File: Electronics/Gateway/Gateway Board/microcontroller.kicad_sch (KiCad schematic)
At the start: 57 parts, among them IC301 STM32H723ZGT6, IC302 TJA1057GT/3, IC303 TJA1057GT/3, IC304 TJA1057GT/3, J301 TC2030, J302 MEM2075-00-140-01-A, J303 TYPE-C-31-M-12, J304 Screw_Terminal_01x02, J305 Screw_Terminal_01x02, J306 Screw_Terminal_01x02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

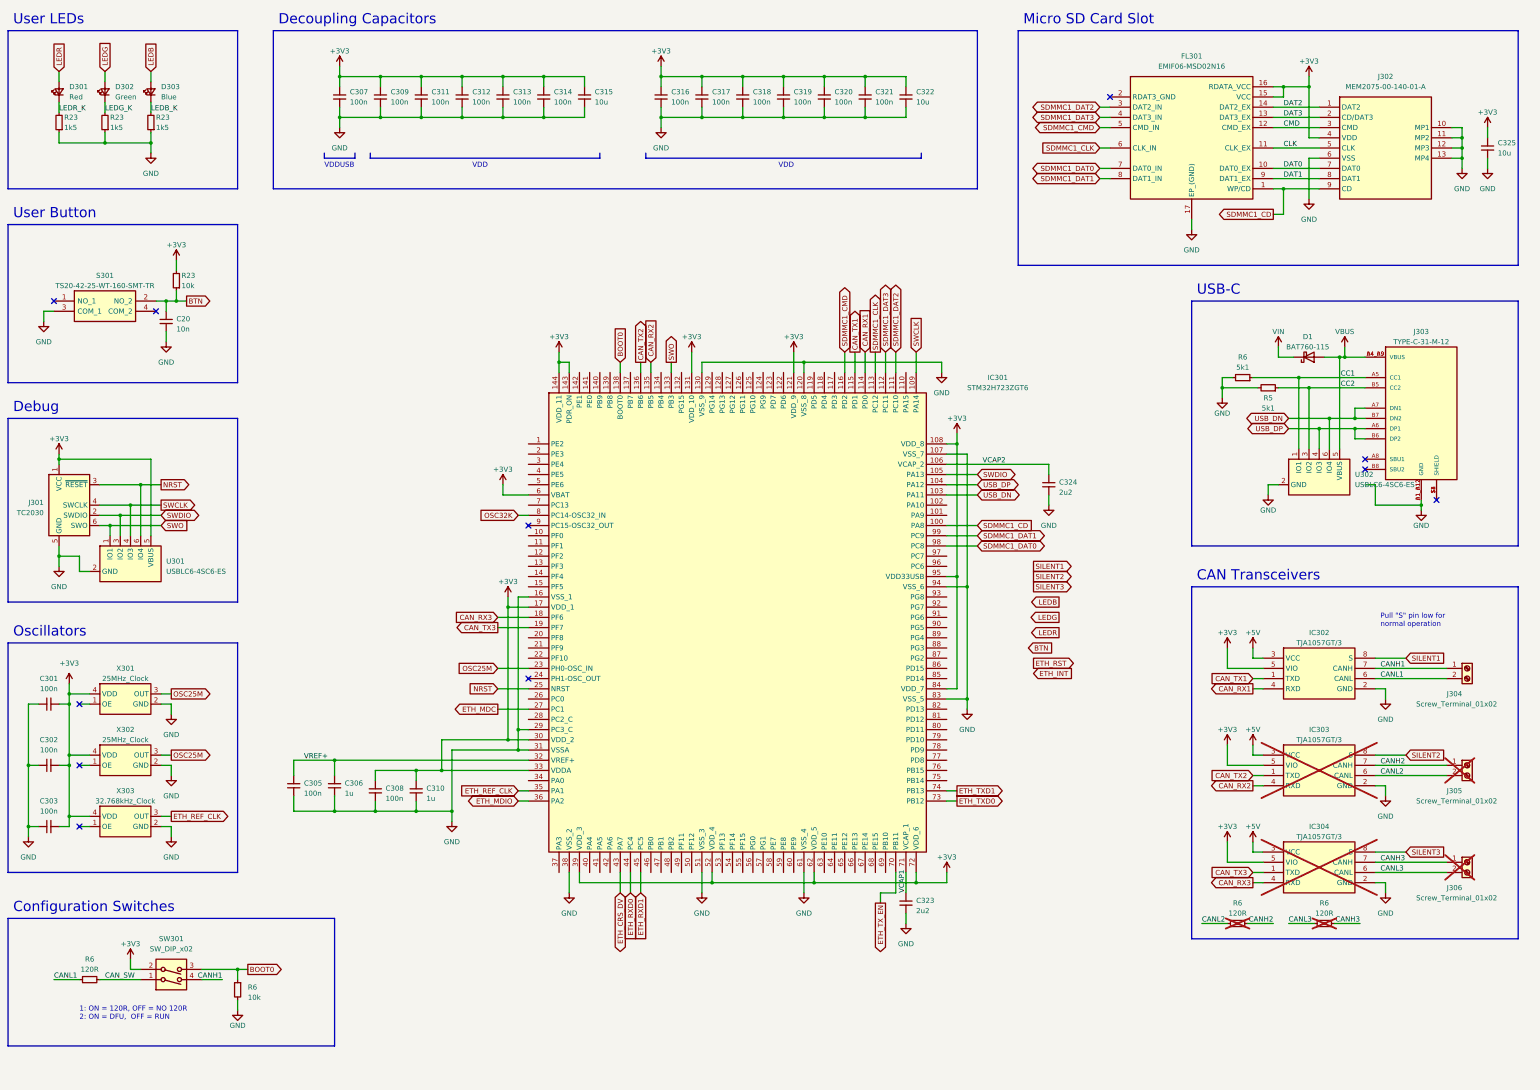
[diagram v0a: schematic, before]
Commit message: Schematic updates
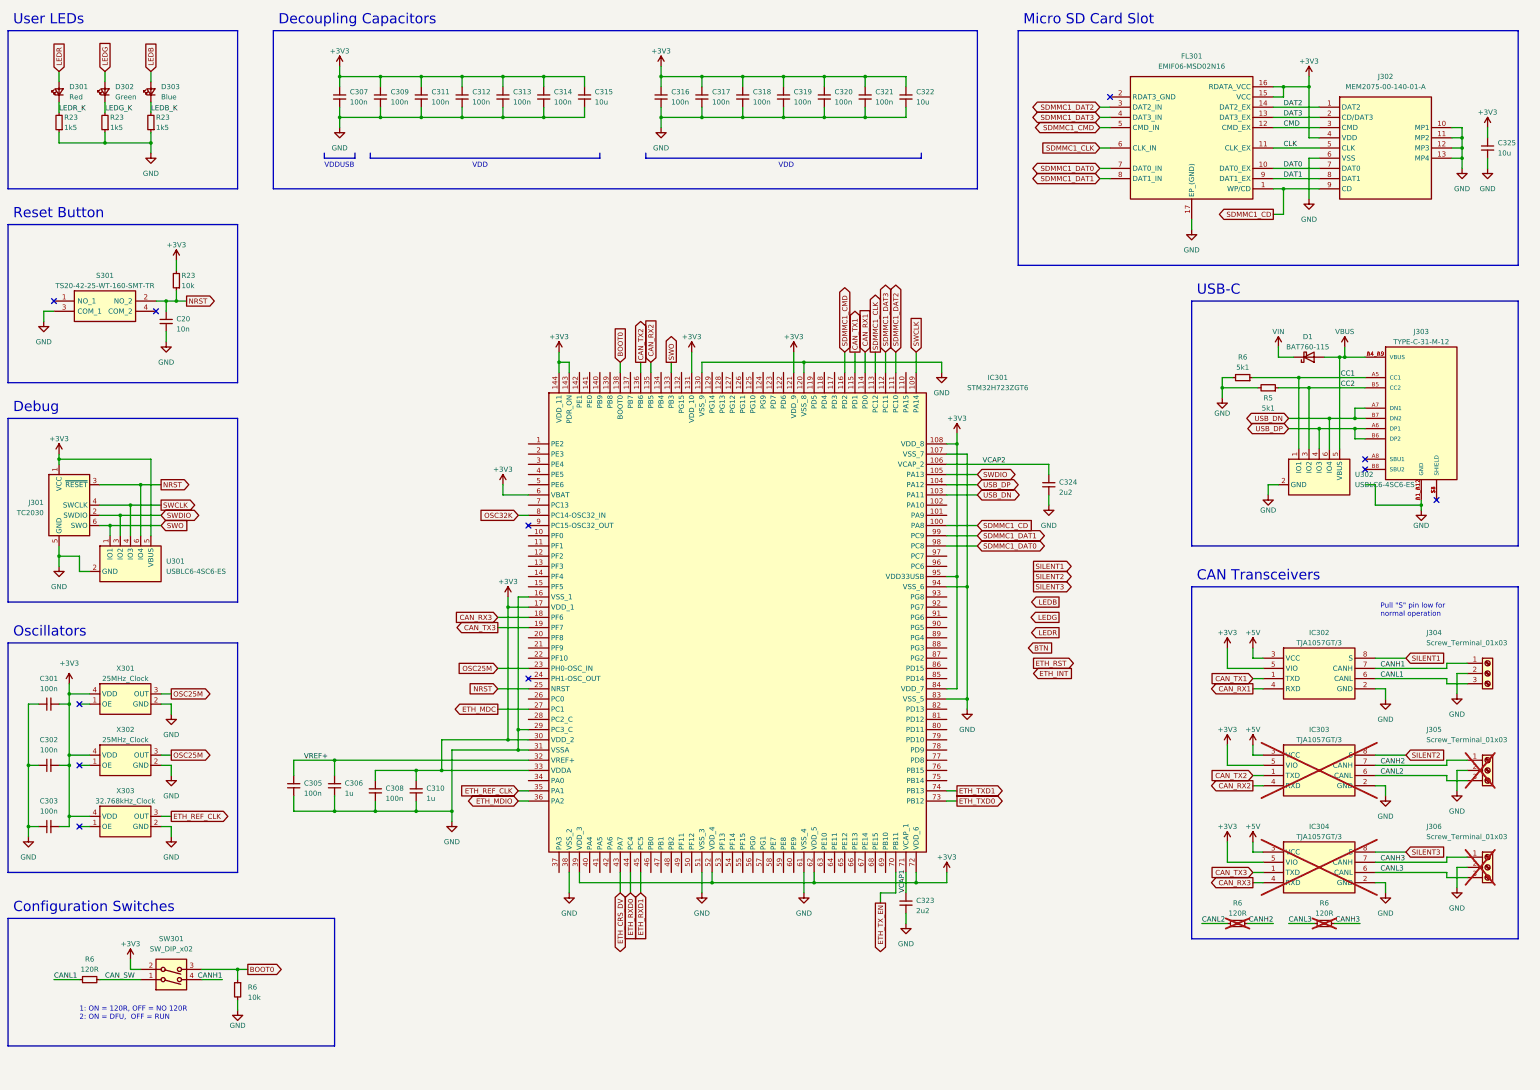
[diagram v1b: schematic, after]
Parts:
- removed J304, J305, J306: Screw_Terminal_01x02, TerminalBlock:TerminalBlock_bornier-2_P5.08mm, symbol Connector:Screw_Terminal_01x02
- added J304, J305, J306: Screw_Terminal_01x03, TerminalBlock:TerminalBlock_bornier-3_P5.08mm, symbol Connector:Screw_Terminal_01x03
- FL301: footprint EMIF06MSD02N16 -> MSL Footprints:EMIF06MSD02N16
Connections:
- net BTN: no longer C20.1, R23.1, S301.2 (NO_2)
- net CANH1: now also J304.1 (Pin_1)
- net CANH2: now also J305.1 (Pin_1)
- net CANH3: now also J306.1 (Pin_1)
- net CANL1: now also J304.3 (Pin_3)
- net CANL2: now also J305.3 (Pin_3)
- net CANL3: now also J306.3 (Pin_3)
- net GND: now also J304.2 (Pin_2), J305.2 (Pin_2), J306.2 (Pin_2)
- net NRST: now also C20.1, R23.1, S301.2 (NO_2)
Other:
- note added: "Reset Button"
- note removed: "User Button"

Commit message: Gateway board layout complete and routing begun
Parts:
- removed J301: TC2030, Connector:Tag-Connect_TC2030-IDC-FP_2x03_P1.27mm_Vertical, symbol Connector:Conn_ARM_SWD_TagConnect_TC2030
- removed J304, J305, J306: Screw_Terminal_01x03, TerminalBlock:TerminalBlock_bornier-3_P5.08mm, symbol Connector:Screw_Terminal_01x03
- removed X301: 25MHz_Clock, Oscillator:Oscillator_SMD_Abracon_ASE-4Pin_3.2x2.5mm_HandSoldering, symbol MSL_Symbols:25MHz_Clock
- added C20: 10n, Capacitor_SMD:C_0402_1005Metric, symbol Device:C_Small
- added C327: 100n, Capacitor_SMD:C_0402_1005Metric, symbol Device:C_Small
- added J301: TC2030, MSL Footprints:Tag-Connect_TC2030-IDC-FP_2x03_P1.27mm_Vertical, symbol MSL_Symbols:TC2030
- added J304, J305, J306: Pluggable_Terminal_01x03, MSL Footprints:Pluggable_terminal-3_P5.08mm, symbol MSL_Symbols:Pluggable_Terminal_01x03
- added R23: 10k, Resistor_SMD:R_0402_1005Metric, symbol Device:R_Small
- added S302: TS20-42-25-WT-160-SMT-TR, MSL Footprints:TS204225WT160SMTTRMSL, symbol TS20-42-25-WT-160-SMT-TR-MSL:TS20-42-25-WT-160-SMT-TR
- added X301: 50MHz_Clock, Oscillator:Oscillator_SMD_Abracon_ASE-4Pin_3.2x2.5mm_HandSoldering, symbol MSL_Symbols:50MHz_Clock
- IC303, IC304, R6: now fitted; now in the parts list
- U301: now not fitted; now left out of the parts list
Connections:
- net BOOT0: now also SW301.4; no longer SW301.3
- net BTN: now also C20.1, R23.1, S302.2 (NO_2)
- net CANH1: now also R6.1, J304.1 (Pin_1); no longer SW301.4
- net CANH2: now also J305.1 (Pin_1)
- net CANH3: now also J306.1 (Pin_1)
- net CANL1: now also SW301.3, J304.3 (Pin_3); no longer R6.1
- net CANL2: now also J305.3 (Pin_3)
- net CANL3: now also J306.3 (Pin_3)
- net CAN_SW: now also SW301.2; no longer SW301.1
- net ETH_REF_CLK: now also X301.3 (OUT); no longer X303.3 (OUT)
- net GND: now also C20.2, C327.2, J301.5 (GND), J304.2 (Pin_2), J305.2 (Pin_2), J306.2 (Pin_2), S302.3 (COM_1), X301.2 (GND)
- net NRST: now also J301.3 (~{RESET})
- net OSC32K: now also X303.3 (OUT)
- net SWCLK: now also J301.4 (SWCLK)
- net SWDIO: now also J301.2 (SWDIO)
- net SWO: now also J301.6 (SWO)
- net +3V3 renamed +3.3V
- net +3.3V: now also SW301.1, C327.1, J301.1 (VCC), R23.2, X301.4 (VDD); no longer SW301.2
- no-connect marks 11 -> 13
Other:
- note added: "User Button"
- note added: "VBAT"
- moved on the sheet: C307, C309, C311, C312, C313, C314, C315, C316, C317, C318, C319, C320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

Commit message: Sensor hub board done
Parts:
- added C20 (x6): 100n, Capacitor_SMD:C_0402_1005Metric, symbol Device:C_Small
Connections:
- net +3.3V: now also C20.1, C20.1, C20.1
- net +5V: now also C20.1, C20.1, C20.1
- net BTN: now also IC301.123 (PD7)
- net CC1: now also U302.3 (IO2); no longer U302.1 (IO1)
- net CC2: now also U302.1 (IO1); no longer U302.3 (IO2)
- net ETH_INT: now also IC301.14 (PF4)
- net ETH_RST: now also IC301.13 (PF3)
- net GND: now also C20.2, C20.2, C20.2, C20.2, C20.2, C20.2; no longer J302.10 (MP1), J302.11 (MP2), J302.12 (MP3), J302.13 (MP4)
- net LEDB: now also IC301.12 (PF2)
- net LEDG: now also IC301.10 (PF0)
- net LEDR: now also IC301.11 (PF1)
- net SILENT1: now also IC301.47 (PB1)
- net SILENT2: now also IC301.64 (PE11)
- net SILENT3: now also IC301.65 (PE12)
- now unconnected: J303.S1 (SHIELD), J303.S2 (SHIELD), J303.S3 (SHIELD), J303.S4 (SHIELD)
- no-connect marks 13 -> 93
